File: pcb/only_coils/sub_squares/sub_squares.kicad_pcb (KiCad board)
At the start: 4 copper layers, 70 x 50 mm, 8 parts, among them J2 Conn_01x06_Pin, J4 Conn_01x03_Pin

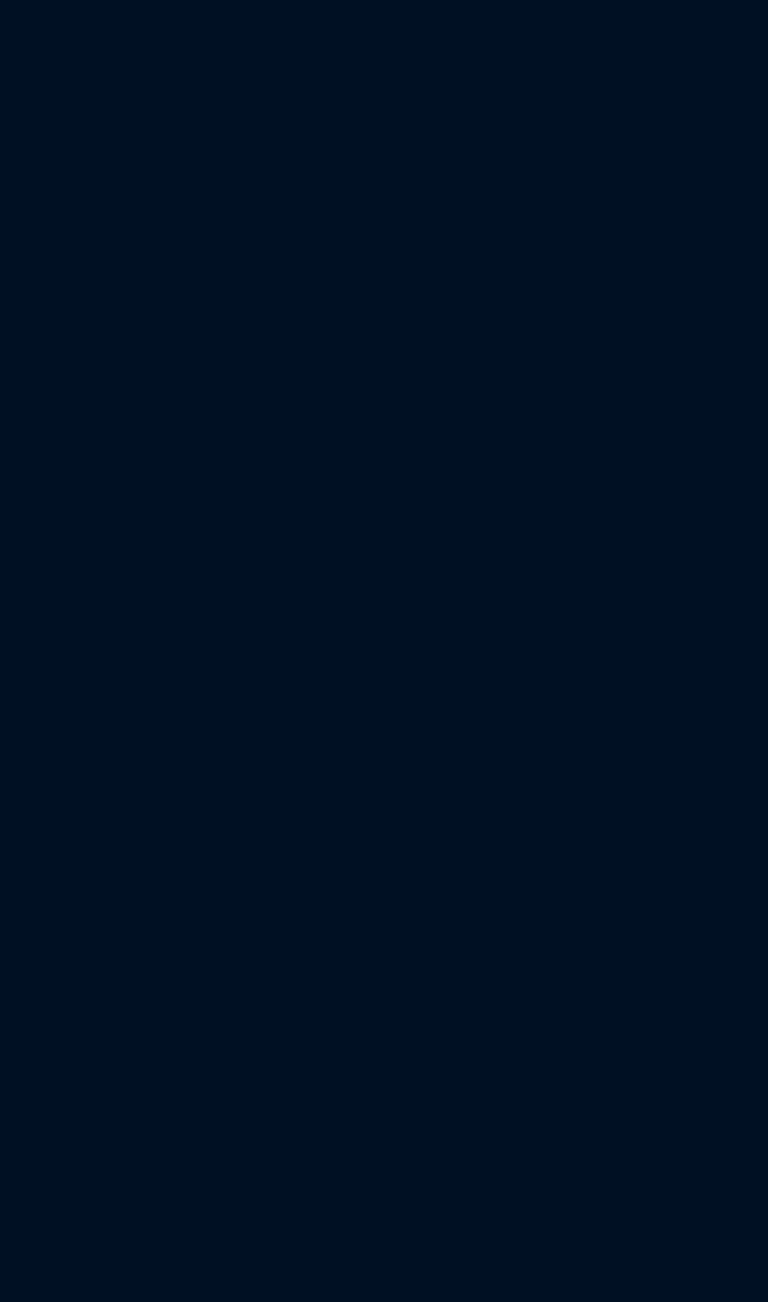
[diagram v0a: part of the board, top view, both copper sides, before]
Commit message: Added poster pptx and pdf
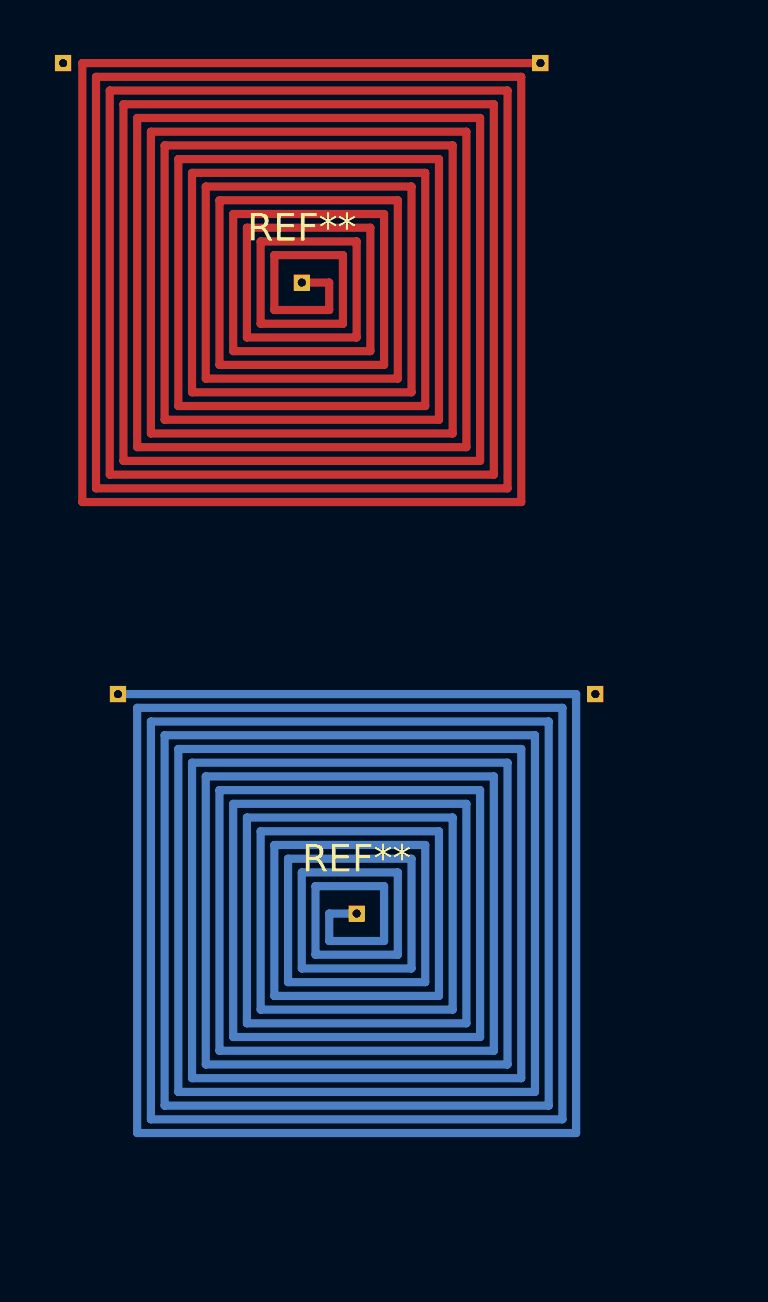
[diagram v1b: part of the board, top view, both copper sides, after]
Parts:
- added REF**: coil, coil, F.Cu at (41.5, 53.0)
- added REF**: coil, coil, F.Cu at (39.5, 30.0)
